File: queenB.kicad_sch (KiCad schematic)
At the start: 188 parts, among them J1 USB4085-GF-A, J2 53048-0310, J3 SFH11-PBPC-D17-ST-BK, J4 TC2030, J5 TC2030, J6 MEM2061-01-188-00-A, SW1 JS202011AQN, SW2 JS202011AQN, SW3 JS202011AQN, U1 BQ24192IRGER, U2 RT5760CHGH6F, U3 CC2500RGPR, U5 STM32H743IIT6, X2 26MHz, X3 S3D26.000000B20F30T

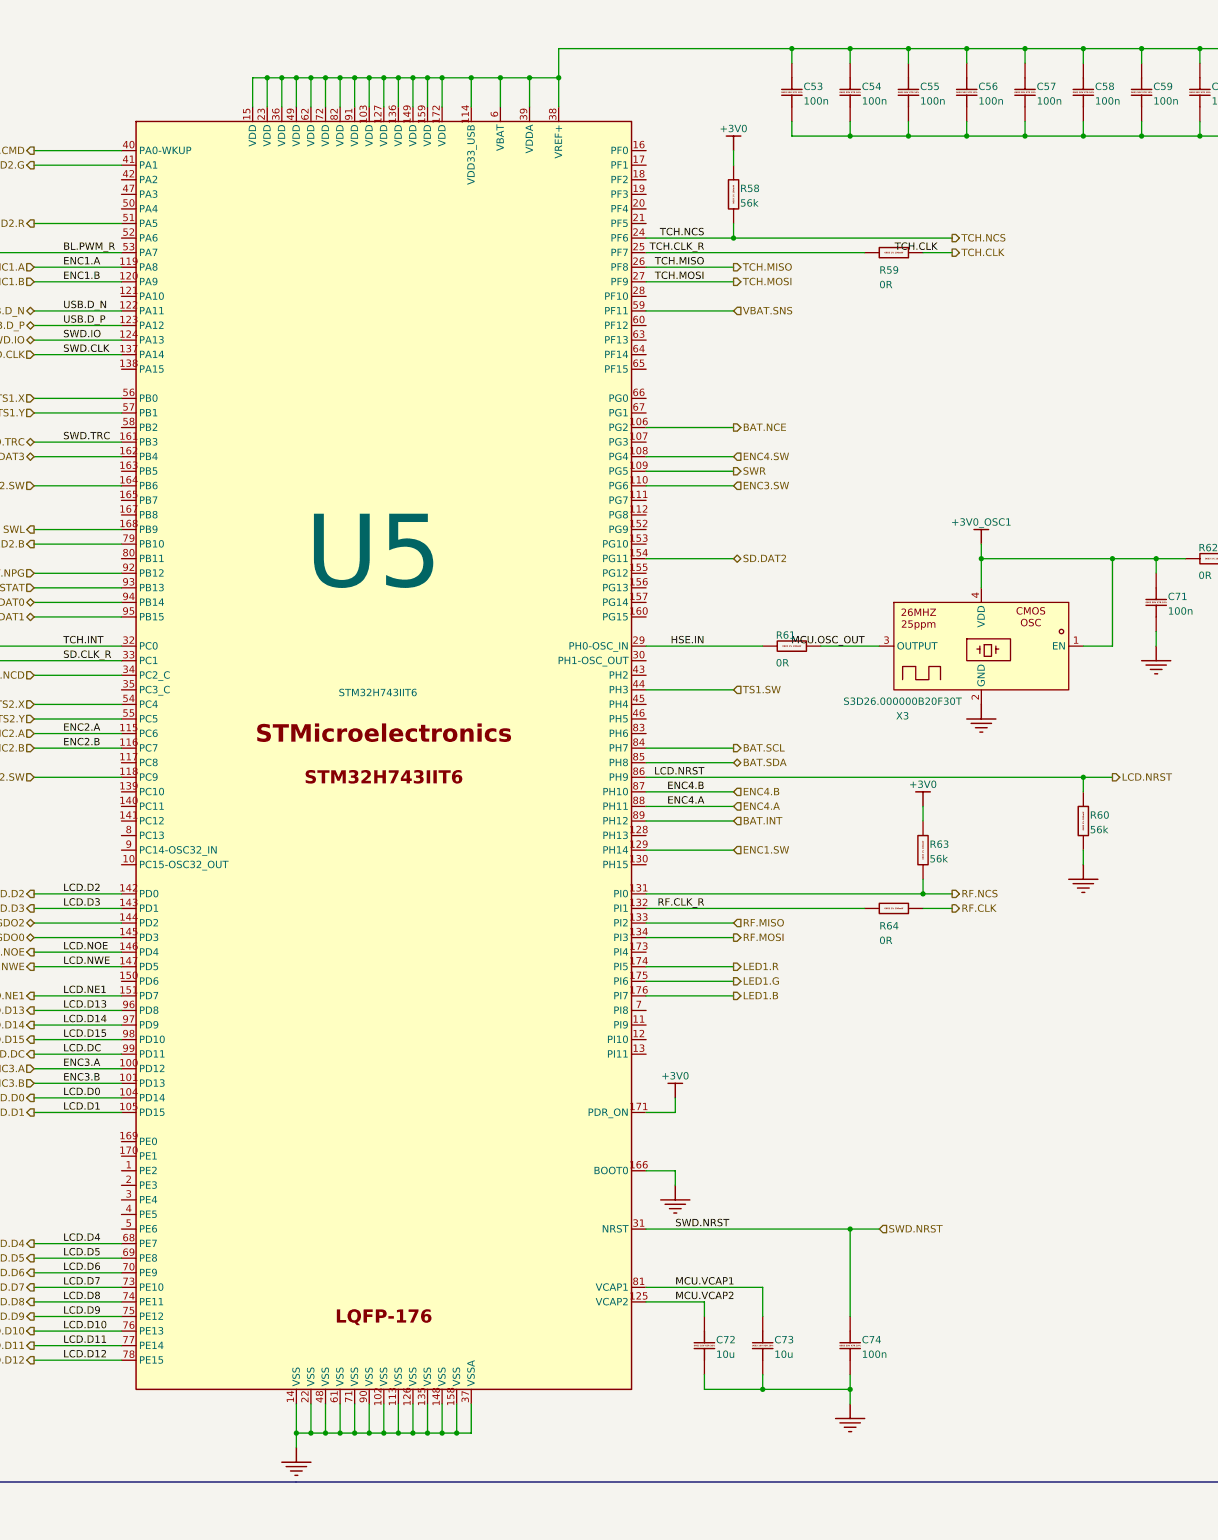
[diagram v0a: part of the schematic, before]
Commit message: Addedd square to tell where i fixed the footprints
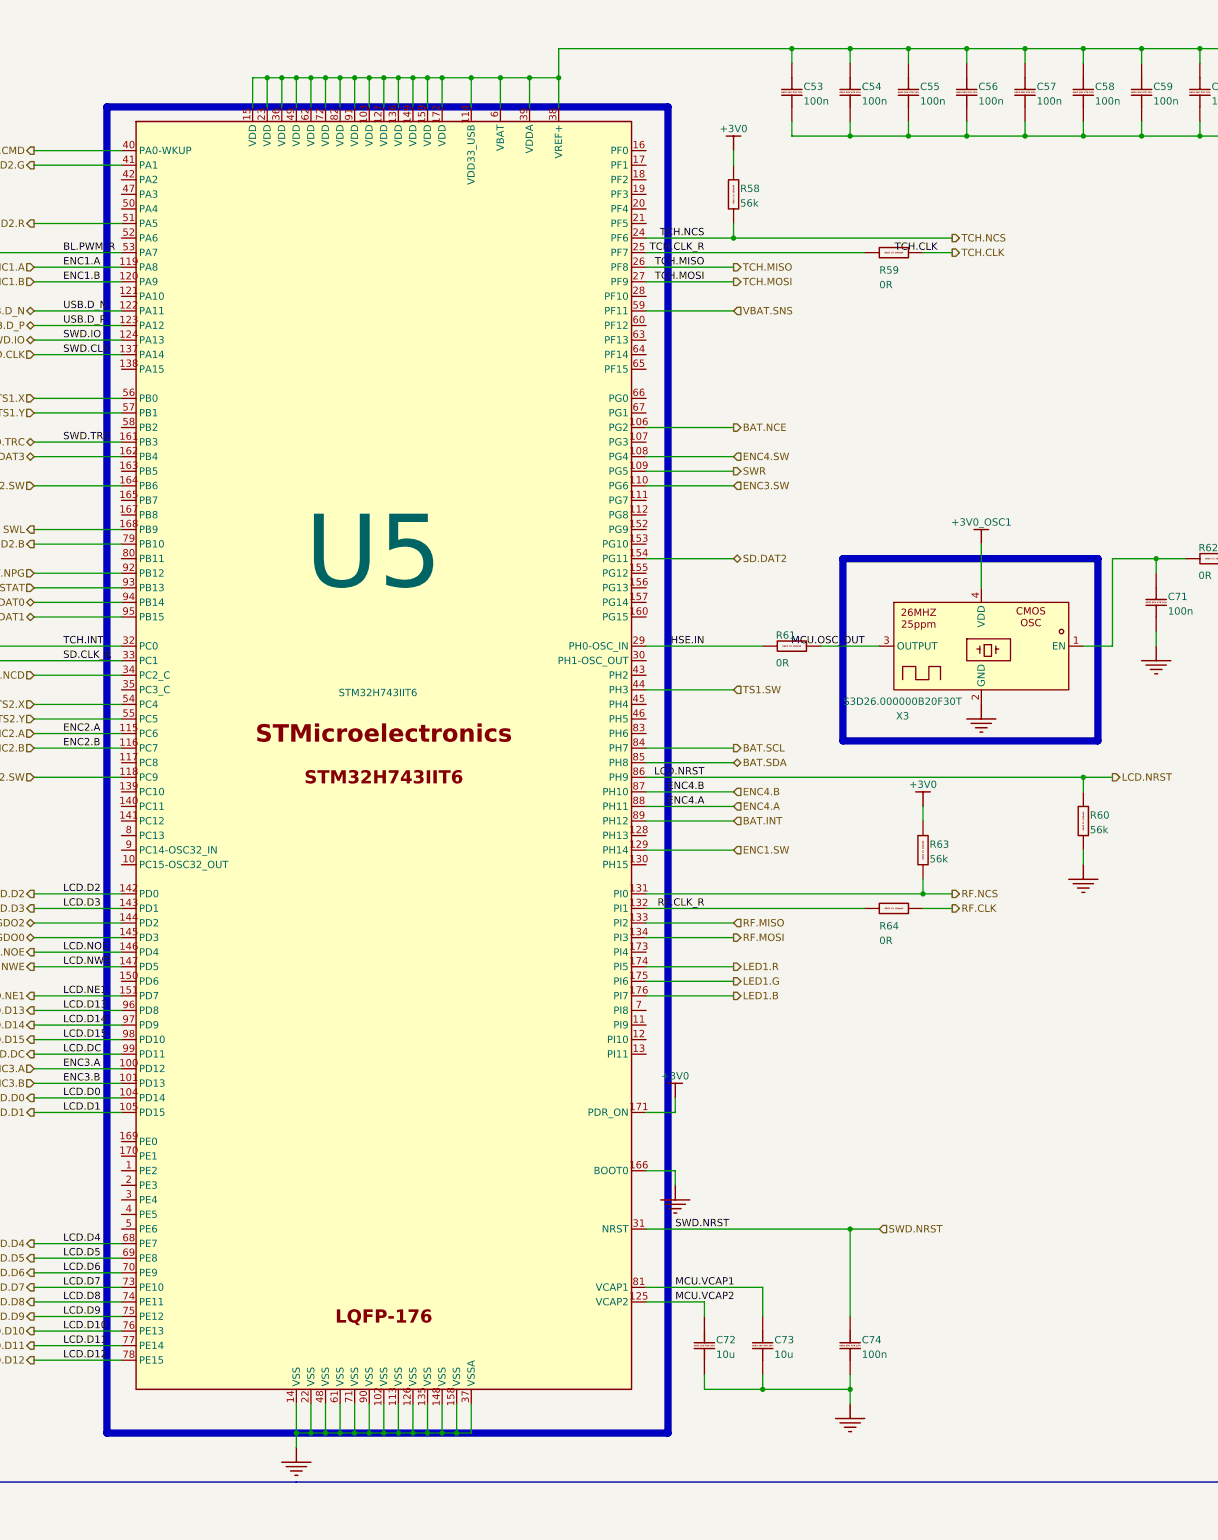
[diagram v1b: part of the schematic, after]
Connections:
- net +3V0_OSC1: no longer C71.1, R62.1, X3.1 (EN)
- new net: C71.1, R62.1, X3.1 (EN)
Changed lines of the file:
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@@
 	)
 	(junction
-		(at 264.16 420.37)
-		(diameter 0)
-		(color 0 0 0 0)
-	)
-	(junction
 		(at 200.66 139.3444)
 		(diameter 0)
@@
 	)
 	(junction
-		(at 241.3 420.37)
-		(diameter 0)
-		(color 0 0 0 0)
-	)
-	(junction
 		(at 248.92 331.47)
 		(diameter 0)
@@
 	(wire
 		(pts
-			(xy 241.3 420.37) (xy 241.3 425.45)
+			(xy 241.3 417.83) (xy 241.3 425.45)
 		)
 		(stroke
@@
 	(wire
 		(pts
-			(xy 241.3 420.37) (xy 264.16 420.37)
-		)
-		(stroke
-			(width 0)
-			(type default)
-		)
-	)
-	(wire
-		(pts
 			(xy 76.2 514.35) (xy 91.44 514.35)
 		)
@@
 	(wire
 		(pts
-			(xy 241.3 417.83) (xy 241.3 420.37)
-		)
-		(stroke
-			(width 0)
-			(type default)
-		)
-	)
-	(wire
-		(pts
 			(xy 693.42 202.8444) (xy 688.34 202.8444)
 		)
@@
 		)
 	)
+	(rectangle
+		(start 217.17 420.37)
+		(end 261.62 452.12)
+		(stroke
+			(width 1.27)
+			(type default)
+			(color 255 16 12 1)
+		)
+		(fill
+			(type none)
+		)
+	)
+	(rectangle
+		(start 88.9 341.63)
+		(end 186.69 572.77)
+		(stroke
+			(width 1.27)
+			(type default)
+			(color 255 16 12 1)
+		)
+		(fill
+			(type none)
+		)
+	)

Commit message: Added 100nf
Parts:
- added C81: CC0402JRX7R7BB104, easyeda2kicad:C0402, symbol easyeda2kicad_local:CC0402JRX7R7BB104
- C20, C23, C54, C55, C56, C57, C58, C59, C60, C61, C62, C63, C64, C65, C66, C67, C68, C69, C77, C78: footprint CAP_0603 -> easyeda2kicad:C0402; symbol queenB-altium-import:root_3_mirrored_CC0603KRX7R9BB104 -> easyeda2kicad_local:CC0402JRX7R7BB104; LCSC Part (none) -> C541464
- U5: footprint easyeda2kicad:LQFP-176_L24.0-W24.0-P0.50-LS26.0-BL -> easyeda2kicad_local:LQFP-176_L24.0-W24.0-P0.50-LS26.0-BL
- X3: footprint easyeda2kicad_script2:OSC-SMD_4P-L3.2-W2.5-BL_SIT8008BI -> easyeda2kicad_local:OSC-SMD_4P-L3.2-W2.5-BL_SIT8008BI
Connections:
- net +3V0: now also C54.2, C55.2, C56.2, C57.2, C58.2, C59.2, C60.2, C61.2, C62.2, C63.2, C64.2, C65.2, C66.2, C67.2, C68.2, C69.2; no longer C54.1, C55.1, C56.1, C57.1, C58.1, C59.1, C60.1, C61.1, C62.1, C63.1, C64.1, C65.1, C66.1, C67.1, C68.1, C69.1
- net GND: now also C54.1, C55.1, C56.1, C57.1, C58.1, C59.1, C60.1, C61.1, C62.1, C63.1, C64.1, C65.1, C66.1, C67.1, C68.1, C69.1; no longer C23.2, C54.2, C55.2, C56.2, C57.2, C58.2, C59.2, C60.2, C61.2, C62.2, C63.2, C64.2, C65.2, C66.2, C67.2, C68.2, C69.2, C77.2, C78.2
- net SWL: no longer C77.1
- net SWR: no longer C78.1
- net TS2.SW: no longer C23.1

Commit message: Added rotory encoder
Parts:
- removed C1, C12, C18, C19, C2, C21, C22, C41, C42, C43, C44, C45, C46, C47, C48, C49, C50, C51, C52, C53, C71, C74, C76: 100n, CAP_0603, symbol queenB-altium-import:root_3_CC0603KRX7R9BB104
- removed C10, C11, C13, C14, C15, C16, C17, C3, C38, C39, C4, C40, C6, C7, C8, C9: 10u, PhilsLab_Footprints_Passive.PcbLib:CAP_0805, symbol queenB-altium-import:root_3_CC0805KKX5R8BB106
- removed C20, C23, C54, C55, C56, C57, C58, C59, C60, C61, C62, C63, C64, C65, C66, C67, C68, C69: 100n, easyeda2kicad:C0402, symbol easyeda2kicad_local:CC0402JRX7R7BB104
- removed C24, C25, C26, C27, C28, C29, C30, C31: 100n, PhilsLab_Footprints_Passive.PcbLib:CAP_0603, symbol queenB-altium-import:root_3_CC0603KRX7R9BB104
- removed C5: 100n, CAP_0603, symbol queenB-altium-import:root_0_CC0603KRX7R9BB104
- removed C70, C75: 10u, PhilsLab_Footprints_Passive.PcbLib:CAP_0805, symbol queenB-altium-import:root_3_mirrored_CC0805KKX5R8BB106
- removed C72, C73: 10u, CAP_0603, symbol queenB-altium-import:root_3_CC0603MRX5R6BB106
- removed C79, C80: 100n, CAP_0603, symbol queenB-altium-import:root_2_CC0603KRX7R9BB104
- removed C81: CC0402JRX7R7BB104, easyeda2kicad:C0402, symbol easyeda2kicad_local:CC0402JRX7R7BB104
- removed D1: USBLC6-2P6, PhilsLab_Footprints_IC.PcbLib:SOT-666, symbol queenB-altium-import:root_0_USBLC6-2P6
- removed J1: USB4085-GF-A, PhilsLab_Footprints_Connector.PcbLib:USB4085-GF-A, symbol queenB-altium-import:root_0_USB4085-GF-A
- removed J2: 53048-0310, PhilsLab_Footprints_Connector.PcbLib:53048-0310, symbol queenB-altium-import:root_0_53048-0310
- removed J3: SFH11-PBPC-D17-ST-BK, PhilsLab_Footprints_Connector.PcbLib:SFH11-PBPC-D17-ST-BK, symbol queenB-altium-import:root_0_SFH11-PBPC-D17-ST-BK
- removed L1, L2: 2u2, PhilsLab_Footprints_Passive.PcbLib:XAL4020, symbol queenB-altium-import:root_0_XAL4020-222MEC
- removed R1: 0R, PhilsLab_Footprints_Passive.PcbLib:RES_0603, symbol queenB-altium-import:root_0_RC0603FR-070RL
- removed R10, R11: 220k, PhilsLab_Footprints_Passive.PcbLib:RES_0603, symbol queenB-altium-import:root_0_RC0603FR-07220KL
- removed R12, R16, R17, R18: 220k, PhilsLab_Footprints_Passive.PcbLib:RES_0603, symbol queenB-altium-import:root_1_RC0603FR-07220KL
- removed R13, R4, R8, R9: 56k, PhilsLab_Footprints_Passive.PcbLib:RES_0603, symbol queenB-altium-import:root_1_RC0603FR-0756KL
- removed R14, R19: 56k, PhilsLab_Footprints_Passive.PcbLib:RES_0603, symbol queenB-altium-import:root_1_mirrored_RC0603FR-0756KL
- removed R15: 270R, PhilsLab_Footprints_Passive.PcbLib:RES_0603, symbol queenB-altium-import:root_1_mirrored_RC0603FR-07270RL
- removed R2, R3, R5, R6, R7: 5k1, PhilsLab_Footprints_Passive.PcbLib:RES_0603, symbol queenB-altium-import:root_1_RC0603FR-075K1L
- removed SW1: JS202011AQN, PhilsLab_Footprints_Control.PcbLib:JS202011AQN, symbol queenB-altium-import:root_0_mirrored_JS202011AQN
- removed U1: BQ24192IRGER, PhilsLab_Footprints_IC.PcbLib:VQFN-24, symbol queenB-altium-import:root_0_BQ24192IRGER
- removed U2: RT5760CHGH6F, PhilsLab_Footprints_IC.PcbLib:SOT-563, symbol queenB-altium-import:root_0_RT5760CHGH6F
- removed X2: 26MHz, PhilsLab_Footprints_Misc.PcbLib:XTAL_2520, symbol queenB-altium-import:root_0_ECS-2520MVQ-260-CN-TR
- added C1, C2: CL10B105KA8NNNC, easyeda2kicad:C0603, symbol easyeda2kicad_script3:CL10B105KA8NNNC
- added C10, C11, C12, C13, C14, C15, C16, C17, C18, C19, C20, C21, C22, C23, C24, C25, C26, C27, C28, C29, C30, C31, C4, C41, C42, C43, C44, C45, C46, C47, C48, C49, C5, C50, C51, C52, C53, C54, C55, C56, C57, C58, C59, C6, C63, C7, C8, C9: CC0402KRX7R7BB104, easyeda2kicad_script3:C0402, symbol easyeda2kicad_script3:CC0402KRX7R7BB104
- added C3: CL10B105KA8NNNC, easyeda2kicad_script3:C0603, symbol easyeda2kicad_script3:CL10B105KA8NNNC
- added C38, C60, C61, C62, C64, C65, C66: CL21A106KPFNNNE, easyeda2kicad_script3:C0805, symbol easyeda2kicad_script3:CL21A106KPFNNNE
- added D4, D5, D6, D7: GG0402052R542P, easyeda2kicad_script3:D0402-BI, symbol easyeda2kicad_script3:GG0402052R542P
- added J3: PM254-2-17-Z-8.5, easyeda2kicad_script3:HDR-TH_34P-P2.54-V-F-R2-C17-S2.54-1, symbol easyeda2kicad_script2:PM254-2-17-Z-8.5
- added R75, R76: 0402WGF5101TCE, easyeda2kicad:R0402, symbol easyeda2kicad_script3:0402WGF5101TCE
- added SW1: PEC12R-4120F-S0012-C143801, easyeda2kicad_script3:SW-TH_PEC12R-4120F-S0012, symbol easyeda2kicad_script3:PEC12R-4120F-S0012-C143801
- added U1: LM3940IMP-3.3/NOPB, easyeda2kicad_script3:SOT-223_L6.5-W3.5-P2.30-LS7.0-BR, symbol easyeda2kicad_script3:LM3940IMP-3.3_NOPB
- added U4: CS3225X7R476K160NRL, easyeda2kicad_script3:C1210, symbol easyeda2kicad_script3:CS3225X7R476K160NRL
- added USB1: TYPE-C 16PIN 2MD(073), easyeda2kicad_script3:USB-C-SMD_TYPE-C-6PIN-2MD-073, symbol easyeda2kicad_script3:TYPE-C16PIN2MD(073)
- added X1: S3D26.000000B20F30T, easyeda2kicad_script3:OSC-SMD_4P-L3.2-W2.5-BL_SIT8008BI, symbol easyeda2kicad_script2:S3D26.000000B20F30T
- C77, C78: footprint easyeda2kicad:C0402 -> CAP_0603; symbol easyeda2kicad_local:CC0402JRX7R7BB104 -> queenB-altium-import:root_3_mirrored_CC0603KRX7R9BB104; LCSC Part C541464 -> (none)
- U5: footprint easyeda2kicad_local:LQFP-176_L24.0-W24.0-P0.50-LS26.0-BL -> easyeda2kicad_script3:LQFP-176_L24.0-W24.0-P0.50-LS26.0-BL
- X3: footprint easyeda2kicad_local:OSC-SMD_4P-L3.2-W2.5-BL_SIT8008BI -> easyeda2kicad_script3:OSC-SMD_4P-L3.2-W2.5-BL_SIT8008BI
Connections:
- net +3V0: now also C10.2, C11.2, C12.2, C13.2, C14.2, C15.2, C16.2, C17.2, C24.2, C25.2, C26.2, C27.2, C28.2, C29.2, C5.2, C53.2, C54.2, C55.2, C56.2, C6.2, C60.1, C7.2, C8.2, C9.2, U1.3 (OUT), U4.2
- net +3V0_DISP: now also C64.1, J3.2
- net +3V0_OSC2: now also C30.2, X1.1 (EN), X1.4 (VDD)
- net +3V0_SD: now also C38.1
- net +VBL: now also C65.1, J3.10
- net +VSYS: now also C52.1, C58.1
- net +VSYS_DISP: now also C66.1, J3.34
- net +VUSB: now also C1.2, C2.2, C3.2, D6.2, D7.2, U1.1 (IN), USB1.11 (VBUS), USB1.2 (VBUS)
- net BL.PWM: now also J3.8
- net ENC1.A: now also C41.2
- net ENC1.B: now also C42.2
- net ENC2.A: now also C44.2
- net ENC2.B: now also C45.2
- net ENC2.SW: now also C43.2
- net ENC3.A: now also C48.2
- net ENC3.B: now also C47.2
- net ENC3.SW: now also C46.2
- net ENC4.A: now also C50.2
- net ENC4.B: now also C51.2
- net ENC4.SW: now also C49.2
- net GND: now also C77.2, C78.2, C1.1, C10.1, C11.1, C12.1, C13.1, C14.1, C15.1, C16.1, C17.1, C18.1, C19.1, C2.1, C20.1, C21.1, C22.1, C23.1, C24.1, C25.1, C26.1, C27.1, C28.1, C29.1, C3.1, C30.1, C31.1, C38.2, C4.1, C41.1, C42.1, C43.1, C44.1, C45.1, C46.1, C47.1, C48.1, C49.1, C5.1, C50.1, C51.1, C52.2, C53.1, C54.1, C55.1, C56.1, C57.1, C58.2, C59.1, C6.1, C60.2, C61.2, C62.2, C63.1, C64.2, C65.2, C66.2, C7.1, C8.1, C9.1, D4.1, D5.1, D6.1, D7.1, J3.1, J3.33, J3.9, R75.1, R76.1, U1.2 (GND), U1.4 (GND), U4.1, USB1.1 (GND), USB1.12 (GND), USB1.13 (SHELL), USB1.14 (SHELL), X1.2 (GND)
- net LCD.D0: now also J3.32
- net LCD.D1: now also J3.31
- net LCD.D10: now also J3.22
- net LCD.D11: now also J3.21
- net LCD.D12: now also J3.20
- net LCD.D13: now also J3.19
- net LCD.D14: now also J3.18
- net LCD.D15: now also J3.17
- net LCD.D2: now also J3.30
- net LCD.D3: now also J3.29
- net LCD.D4: now also J3.28
- net LCD.D5: now also J3.27
- net LCD.D6: now also J3.26
- net LCD.D7: now also J3.25
- net LCD.D8: now also J3.24
- net LCD.D9: now also J3.23
- net LCD.DC: now also J3.15
- net LCD.NE1: now also J3.16
- net LCD.NOE: now also J3.13
- net LCD.NRST: now also J3.12
- net LCD.NWE: now also J3.14
- net MCU.VCAP1: now also C61.1
- net MCU.VCAP2: now also C62.1
- net RF.DCOUPL: now also C31.2
- net RF.XOSC_OUT: now also X1.3 (OUTPUT)
- net SD.NCD: now also C59.2
- net SWD.NRST: now also C63.2
- net SWL: now also C77.1
- net SWR: now also C78.1
- net TCH.CLK: now also J3.5
- net TCH.INT: now also J3.7
- net TCH.MISO: now also J3.3
- net TCH.MOSI: now also J3.4
- net TCH.NCS: now also J3.6
- net TS1.SW: now also C19.2
- net TS1.X: now also C18.2
- net TS1.Y: now also C21.2
- net TS2.SW: now also C20.2
- net TS2.X: now also C57.2
- net TS2.Y: now also C22.2
- net USB.D_N: now also D4.2, USB1.5 (DN2), USB1.7 (DN1)
- net USB.D_P: now also D5.2, USB1.6 (DP1), USB1.8 (DP2)
- net at R62.1, X3.1 (EN): now also C4.2
- new net: R76.2, USB1.10 (CC2)
- new net: R75.2, USB1.4 (CC1)
- no-connect marks 16 -> 13
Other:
- note added: "3V3 Buck Converter"
- note added: "Drone Controller"
- note added: "USB_C"
- note removed: "3V0 Buck Converter"
- note removed: "3V7<=VSYS<4V2"
- note removed: "Gain=0.5"
- note removed: "I2C ADDRESS = 0x6B"
- note removed: "QueenB - Drone Controller"
- note removed: "Set ILIM via register!"
- note removed: "USB & Battery Charger"
- note removed: "V=0.6*(1+220/56)=2.96V"
- title: QueenB -> Lampel Remote
- moved on the sheet: ANT1, C32, C33, C34, C35, C36, C37, J6, L3, L4, L5, R24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

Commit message: Added some res
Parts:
- J3: footprint easyeda2kicad_script3:HDR-TH_34P-P2.54-V-F-R2-C17-S2.54-1 -> easyeda2kicad:HDR-TH_34P-P2.54-V-F-R2-C17-S2.54-1
- SW1: footprint easyeda2kicad_script3:SW-TH_PEC12R-4120F-S0012 -> easyeda2kicad:SW-TH_PEC12R-4120F-S0012
- U5: footprint easyeda2kicad_script3:LQFP-176_L24.0-W24.0-P0.50-LS26.0-BL -> easyeda2kicad:LQFP-176_L24.0-W24.0-P0.50-LS26.0-BL
- X1, X3: footprint easyeda2kicad_script3:OSC-SMD_4P-L3.2-W2.5-BL_SIT8008BI -> easyeda2kicad:OSC-SMD_4P-L3.2-W2.5-BL_SIT8008BI
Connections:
- net +3V0: no longer U5.103 (VDD), U5.114 (VDD33_USB), U5.127 (VDD), U5.136 (VDD), U5.149 (VDD), U5.15 (VDD), U5.159 (VDD), U5.171 (PDR_ON), U5.172 (VDD), U5.23 (VDD), U5.36 (VDD), U5.38 (VREF+), U5.39 (VDDA), U5.49 (VDD), U5.6 (VBAT), U5.62 (VDD), U5.72 (VDD), U5.82 (VDD), U5.91 (VDD)
- net +3V0_DISP: no longer J3.2
- net +3V0_OSC1: no longer X3.4 (VDD)
- net +3V0_OSC2: no longer X1.1 (EN), X1.4 (VDD)
- net +VBL: no longer J3.10
- net +VSYS_DISP: no longer J3.34
- net BAT.INT: no longer U5.89 (PH12)
- net BAT.NCE: no longer U5.106 (PG2)
- net BAT.NPG: no longer U5.92 (PB12)
- net BAT.SCL: no longer U5.84 (PH7)
- net BAT.SDA: no longer U5.85 (PH8)
- net BAT.STAT: no longer U5.93 (PB13)
- net BL.PWM: no longer J3.8
- net BL.PWM_R: no longer U5.53 (PA7)
- net ENC1.A: no longer U5.119 (PA8)
- net ENC1.B: no longer U5.120 (PA9)
- net ENC1.SW: no longer U5.129 (PH14)
- net ENC2.A: no longer U5.115 (PC6)
- net ENC2.B: no longer U5.116 (PC7)
- net ENC2.SW: no longer U5.118 (PC9)
- net ENC3.A: no longer U5.100 (PD12)
- net ENC3.B: no longer U5.101 (PD13)
- net ENC3.SW: no longer U5.110 (PG6)
- net ENC4.A: no longer U5.88 (PH11)
- net ENC4.B: no longer U5.87 (PH10)
- net ENC4.SW: no longer U5.108 (PG4)
- net GND: no longer J3.1, J3.33, J3.9, U5.102 (VSS), U5.113 (VSS), U5.126 (VSS), U5.135 (VSS), U5.14 (VSS), U5.148 (VSS), U5.158 (VSS), U5.166 (BOOT0), U5.22 (VSS), U5.37 (VSSA), U5.48 (VSS), U5.61 (VSS), U5.71 (VSS), U5.90 (VSS), X1.2 (GND), X3.2 (GND)
- net HSE.IN: no longer U5.29 (PH0-OSC_IN)
- net LCD.D0: no longer J3.32, U5.104 (PD14)
- net LCD.D1: no longer J3.31, U5.105 (PD15)
- net LCD.D10: no longer J3.22, U5.76 (PE13)
- net LCD.D11: no longer J3.21, U5.77 (PE14)
- net LCD.D12: no longer J3.20, U5.78 (PE15)
- net LCD.D13: no longer J3.19, U5.96 (PD8)
- net LCD.D14: no longer J3.18, U5.97 (PD9)
- net LCD.D15: no longer J3.17, U5.98 (PD10)
- net LCD.D2: no longer J3.30, U5.142 (PD0)
- net LCD.D3: no longer J3.29, U5.143 (PD1)
- net LCD.D4: no longer J3.28, U5.68 (PE7)
- net LCD.D5: no longer J3.27, U5.69 (PE8)
- net LCD.D6: no longer J3.26, U5.70 (PE9)
- net LCD.D7: no longer J3.25, U5.73 (PE10)
- net LCD.D8: no longer J3.24, U5.74 (PE11)
- net LCD.D9: no longer J3.23, U5.75 (PE12)
- net LCD.DC: no longer J3.15, U5.99 (PD11)
- net LCD.NE1: no longer J3.16, U5.151 (PD7)
- net LCD.NOE: no longer J3.13, U5.146 (PD4)
- net LCD.NRST: no longer J3.12, U5.86 (PH9)
- net LCD.NWE: no longer J3.14, U5.147 (PD5)
- net LED1.B: no longer U5.176 (PI7)
- net LED1.G: no longer U5.175 (PI6)
- net LED1.R: no longer U5.174 (PI5)
- net LED2.B: no longer U5.79 (PB10)
- net LED2.G: no longer U5.41 (PA1)
- net LED2.R: no longer U5.51 (PA5)
- net MCU.OSC_OUT: now also U5.118 (PC9); no longer X3.3 (OUTPUT)
- net MCU.VCAP1: no longer U5.81 (VCAP1)
- net MCU.VCAP2: no longer U5.125 (VCAP2)
- net RF.CLK_R: now also U5.100 (PD12); no longer U5.132 (PI1)
- net RF.GDO0: no longer U5.145 (PD3)
- net RF.GDO2: no longer U5.144 (PD2)
- net RF.MISO: no longer U5.133 (PI2)
- net RF.MOSI: no longer U5.134 (PI3)
- net RF.NCS: no longer U5.131 (PI0)
- net RF.XOSC_OUT: no longer X1.3 (OUTPUT)
- net SD.CLK_R: no longer U5.33 (PC1)
- net SD.CMD: no longer U5.40 (PA0-WKUP)
- net SD.DAT0: no longer U5.94 (PB14)
- net SD.DAT1: no longer U5.95 (PB15)
- net SD.DAT2: no longer U5.154 (PG11)
- net SD.DAT3: no longer U5.162 (PB4)
- net SD.NCD: no longer U5.34 (PC2_C)
- net SWD.CLK: now also U5.172 (VDD), U5.176 (PI7); no longer U5.137 (PA14)
- net SWD.IO: no longer U5.124 (PA13)
- net SWD.NRST: no longer U5.31 (NRST)
- net SWD.TRC: no longer U5.161 (PB3)
- net SWL: no longer U5.168 (PB9)
- net SWR: no longer U5.109 (PG5)
- net TCH.CLK: no longer J3.5
- net TCH.CLK_R: no longer U5.25 (PF7)
- net TCH.INT: no longer J3.7, U5.32 (PC0)
- net TCH.MISO: no longer J3.3, U5.26 (PF8)
- net TCH.MOSI: no longer J3.4, U5.27 (PF9)
- net TCH.NCS: no longer J3.6, U5.24 (PF6)
- net TS1.SW: no longer U5.44 (PH3)
- net TS1.X: no longer U5.56 (PB0)
- net TS1.Y: no longer U5.57 (PB1)
- net TS2.SW: no longer U5.164 (PB6)
- net TS2.X: no longer U5.54 (PC4)
- net TS2.Y: no longer U5.55 (PC5)
- net USB.D_N: no longer U5.122 (PA11)
- net USB.D_P: no longer U5.123 (PA12)
- net VBAT.SNS: no longer U5.59 (PF11)
- net at C4.2, R62.1: no longer X3.1 (EN)
